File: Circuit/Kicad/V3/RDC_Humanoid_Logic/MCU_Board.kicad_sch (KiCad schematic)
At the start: 1 part, among them U3 NUCLEO-H755ZI-Q_Zio

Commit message: logic V3のトランジスタアレイ周りを修正
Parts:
- U3: board datasheet (none) -> https://www.st.com/resource/en/user_manual/dm00499171.pdf
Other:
- note added: "修正済み"
- note added: "要修正"
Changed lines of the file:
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@@
 	(generator_version "9.0")
 	(paper "A4")
+	(text "要修正"
+		(exclude_from_sim no)
+		(at 74.422 74.168 0)
+		(effects
+			(font
+				(size 1.27 1.27)
+				(thickness 0.254)
+				(bold yes)
+				(color 99 0 0 1)
+			)
+		)
+	)
+	(text "修正済み"
+		(exclude_from_sim no)
+		(at 123.19 42.164 0)
+		(effects
+			(font
+				(size 1.27 1.27)
+				(thickness 0.254)
+				(bold yes)
+				(color 0 99 0 1)
+			)
+		)
+	)
 	(junction
 		(at 63.5 67.31)
@@
 			)
 		)
+		(property "board datasheet" "https://www.st.com/resource/en/user_manual/dm00499171.pdf"
+			(at 95.25 41.91 0)
+			(effects
+				(font
+					(size 1.27 1.27)
+				)
+				(hide yes)
+			)
+		)

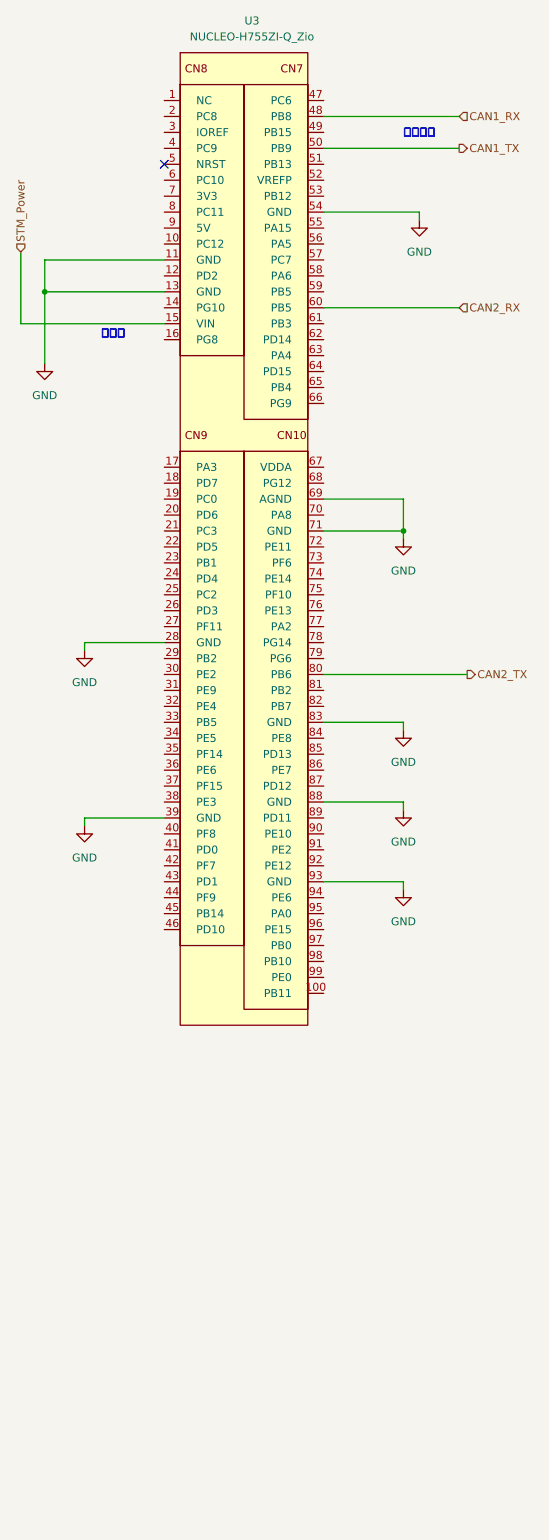
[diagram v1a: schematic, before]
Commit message: Update V3 logic. 回路図の更新完了。PCB途中
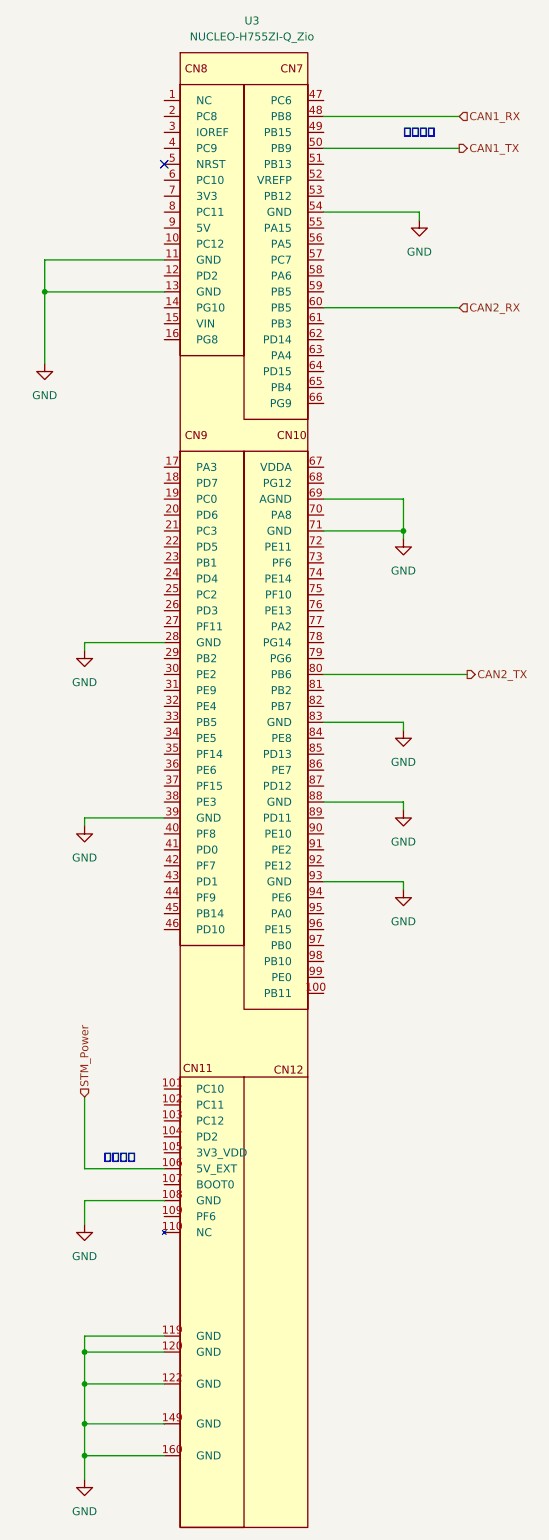
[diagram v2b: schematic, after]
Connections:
- net GND: now also U3.108 (GND), U3.119 (GND), U3.120 (GND), U3.122 (GND), U3.149 (GND), U3.160 (GND)
- net STM_Power: now also U3.106 (5V_EXT); no longer U3.15 (VIN)
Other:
- note removed: "要修正"
